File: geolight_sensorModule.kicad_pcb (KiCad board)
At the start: 2 copper layers, 33 x 24.9 mm, 21 parts, among them P2 ICSP, U1 TCRT5000/L

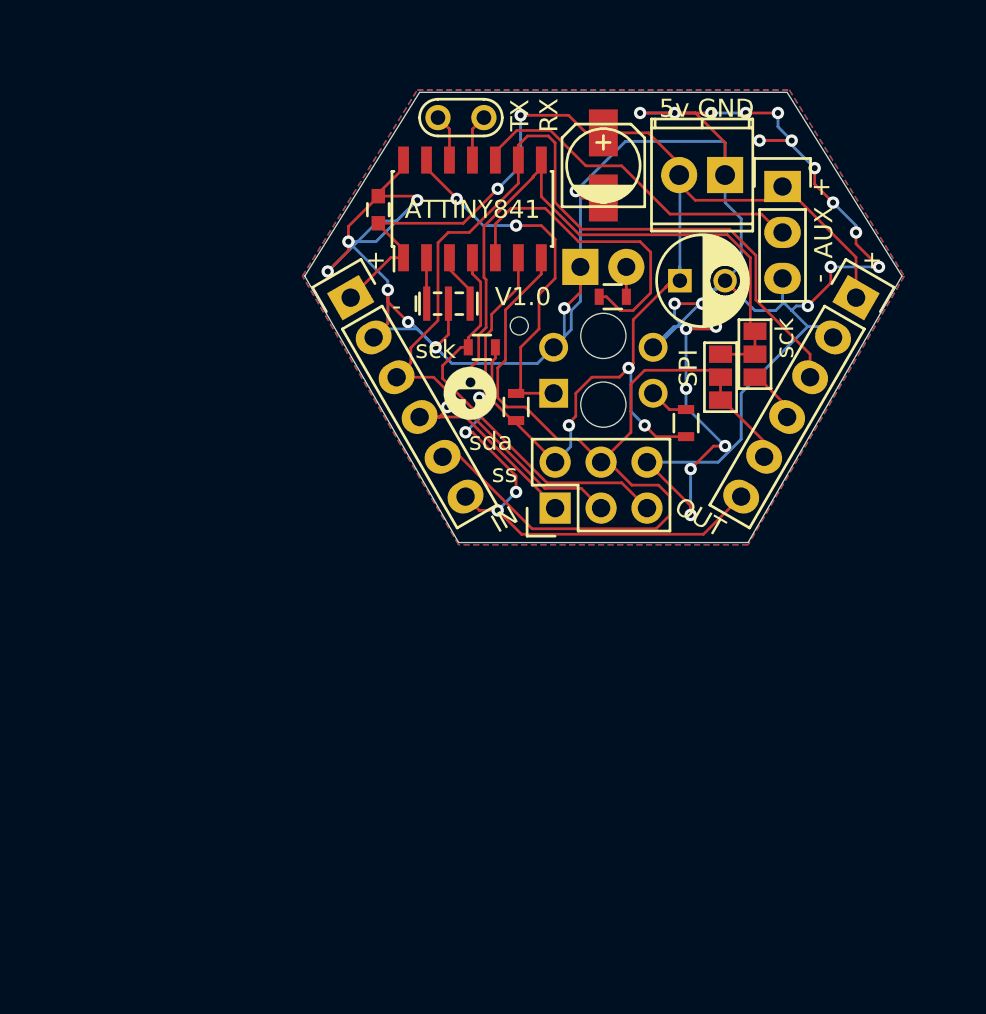
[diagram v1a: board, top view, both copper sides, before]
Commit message: removed empty path cap, changed all 0603 to 0603_handsolder, fixed I2C wiring order, left SPI channels but most likely unused.
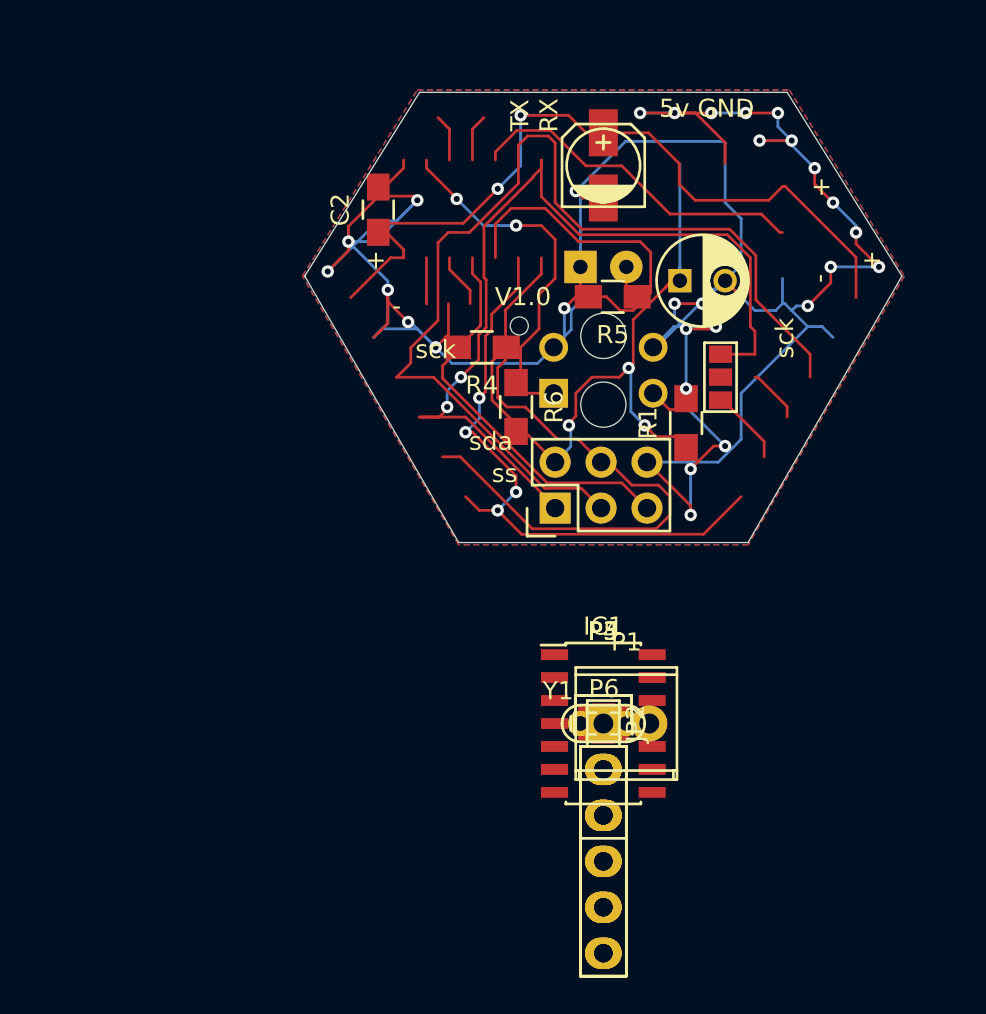
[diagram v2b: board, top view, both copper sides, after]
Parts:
- removed 16M: 16Mhz, Crystals:Resonator_3.2x1.3mm
- removed 5V: 5V, Terminal_Blocks:TerminalBlock_Pheonix_MPT-2.54mm_2pol
- removed ATTINY841: ATTINY841-SSU, Housings_SOIC:SOIC-14_3.9x8.7mm_Pitch1.27mm
- removed AUX: AUX_SENSOR, Pin_Headers:Pin_Header_Straight_1x03
- removed G***: LOGO, Symbols:TI_Logo_F.SilkS_3mm
- removed G***: LOGO, Symbols:TI_Logo_F.SilkS_15mm
- removed IN: IN, Pin_Headers:Pin_Header_Straight_1x06
- removed OUT: OUT, Pin_Headers:Pin_Header_Straight_1x06
- removed SPI: MISO EN, Connect:GS3
- removed tx/rx: UART, Measurement_Points:Test_Point
- added IC1: ATTINY841-SSU, Housings_SOIC:SOIC-14_3.9x8.7mm_Pitch1.27mm, F.Cu at (157.5, 143.4)
- added JP2: OPEN, Connect:GS2, F.Cu at (157.5, 143.4)
- added P1: OPEN, Terminal_Blocks:TerminalBlock_Pheonix_MPT-2.54mm_2pol, F.Cu at (157.5, 143.4)
- added P3, P4: Male Pin Header, Angled (90*), Pin_Headers:Pin_Header_Straight_1x06, F.Cu at (157.5, 143.4)
- added P5: OPEN, Pin_Headers:Pin_Header_Straight_1x03, F.Cu at (157.5, 143.4)
- added P6: OPEN, Measurement_Points:Test_Point, F.Cu at (157.5, 143.4)
- added Y1: 16Mhz, Crystals:Resonator_3.2x1.3mm, F.Cu at (157.5, 143.4)
- C1: value 10-220uF -> OPEN
- C2: footprint Capacitors_SMD:C_0603 -> Capacitors_SMD:C_0805_HandSoldering
- D1: footprint LEDs:LED-3MM -> LEDs:LED-8MM
- JP1: value I2C/SS -> OPEN
- P2: value ICSP -> OPEN
- R1, R5: value 220? -> 220; footprint Resistors_SMD:R_0603 -> Resistors_SMD:R_0805_HandSoldering
- R4, R6: footprint Resistors_SMD:R_0603 -> Resistors_SMD:R_0805_HandSoldering
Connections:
- JP1 pad 2: /SDA/MOSI -> Net-(JP1-Pad2)
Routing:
- net (no net): track 0.00 -> 66.9 mm, vias 0 -> 4
- net /SS: track 33.9 -> 0.00 mm, vias 4 -> 0
- net /AUX: track 19.2 -> 0.00 mm
- net Net-(D1-Pad2): track 1.65 -> 18.9 mm
- net Net-(IC1-Pad5): track 17.6 -> 1.66 mm
- net /SDA/MOSI: track 52.1 -> 40.2 mm
- net Net-(JP2-Pad1): track 3.03 -> 0.00 mm
- net Net-(IC1-Pad3): track 3.01 -> 0.00 mm
- net /TX: track 2.61 -> 0.00 mm
- net /RX: track 2.61 -> 0.00 mm
- net Net-(IC1-Pad2): track 2.55 -> 0.00 mm
- net GND: track 176.4 -> 175.2 mm, vias 30 -> 29
- net Net-(R1-Pad2): vias 0 -> 1

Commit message: 90% complete for 8mm LED. Stopping for change back to 5mm.
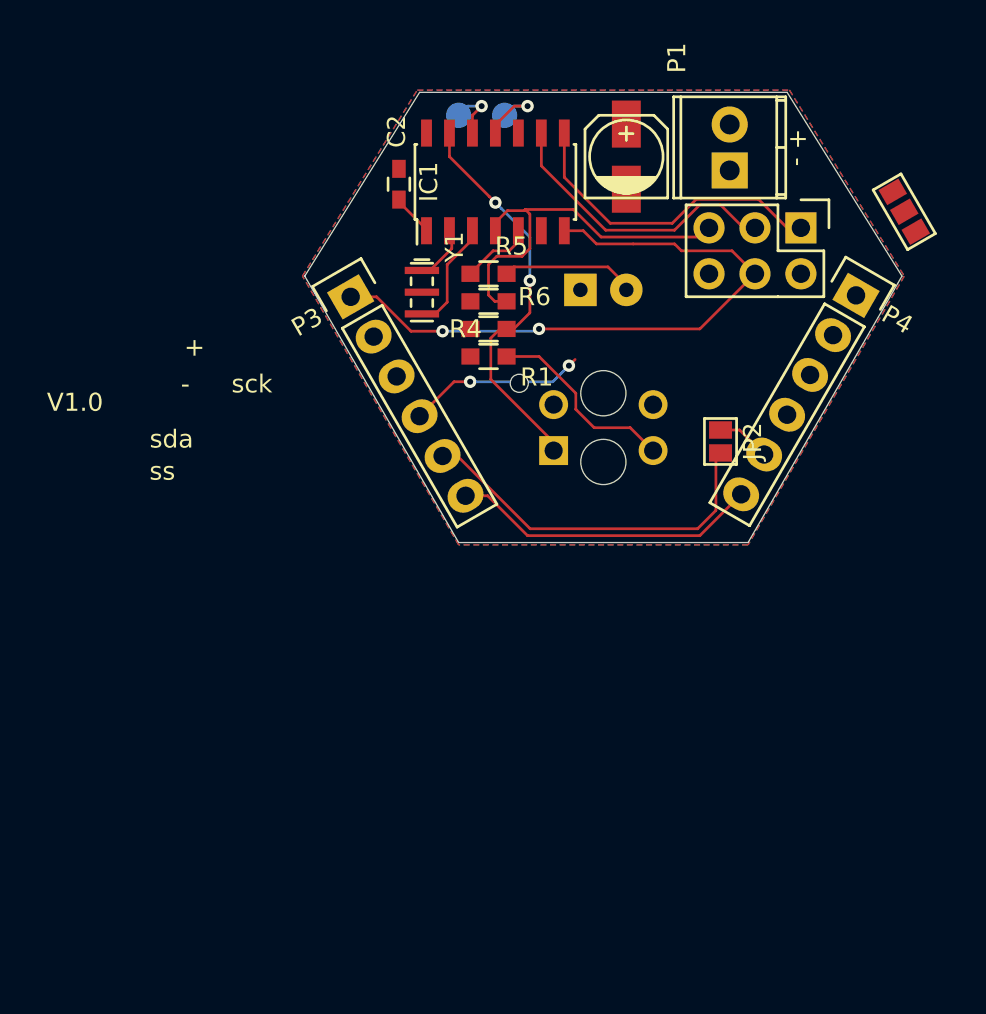
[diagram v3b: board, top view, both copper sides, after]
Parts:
- removed C1: OPEN, Capacitors_ThroughHole:C_Radial_D5_L6_P2.5
- removed P5: OPEN, Pin_Headers:Pin_Header_Straight_1x03
- C2: footprint Capacitors_SMD:C_0805_HandSoldering -> Capacitors_SMD:C_0603_HandSolderingShort
- JP1: value OPEN -> I2C/SPI
- JP2: value OPEN -> MISO_EN
- P1: value OPEN -> 5V inject
- P3: value Male Pin Header, Angled (90*) -> IN
- P4: value Male Pin Header, Angled (90*) -> OUT
- P6: value OPEN -> DEBUG; moved to B.Cu
- R1, R4, R5, R6: footprint Resistors_SMD:R_0805_HandSoldering -> Resistors_SMD:R_0603_HandSolderingShort
- moved P6 34.3 mm to (150.7, 109.7)
- moved P1 31.4 mm to (164.5, 112.8), turned to 90 degrees
- moved IC1 30.5 mm to (151.5, 113.4), turned to 90 degrees
- moved P4 27.5 mm to (171.4, 119.7), turned to 330 degrees
- moved P3 27.4 mm to (143.5, 119.8), turned to 30 degrees
- moved Y1 25.9 mm to (147.4, 119.5), turned to 270 degrees
- moved P2 20.6 mm to (168.4, 116.0), turned to 270 degrees
- moved JP2 16.9 mm to (164.0, 127.8)
- moved JP1 13.7 mm to (174.1, 115.1), turned to 30 degrees
- moved R1 11.5 mm to (151.1, 123.1), turned to 0 degrees
- moved R5 6.99 mm to (151.1, 118.5)
- moved R6 4.58 mm to (151.1, 121.5), turned to 180 degrees
- moved U1 3.17 mm to (157.5, 127.0)
- moved R4 2.57 mm to (151.1, 120.0), turned to 0 degrees
- moved C2 1.81 mm to (146.2, 113.5)
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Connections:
- P4 pad 1: /SCK/SCL -> Net-(JP1-Pad2)
- P4 pad 4: Net-(JP1-Pad2) -> /SCK/SCL
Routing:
- net GND: track 175.2 -> 0.00 mm, vias 29 -> 0
- net +5V: track 79.8 -> 2.35 mm, vias 5 -> 0
- net (no net): track 66.9 -> 0.00 mm, vias 4 -> 0
- net /SCK/SCL: track 56.6 -> 26.1 mm, vias 0 -> 2
- net /SS: track 0.00 -> 17.6 mm
- net Net-(D1-Pad2): track 18.9 -> 7.45 mm
- net /MISO: track 49.7 -> 38.3 mm, vias 2 -> 0
- net Net-(R1-Pad2): track 2.20 -> 10.8 mm, vias 1 -> 0
- net Net-(IC1-Pad3): track 0.00 -> 6.19 mm
- net /SDA/MOSI: track 40.2 -> 36.0 mm, vias 0 -> 2
- net /RX: track 0.00 -> 4.14 mm, vias 0 -> 1
- net Net-(IC1-Pad2): track 0.00 -> 3.19 mm
- net /TX: track 0.00 -> 3.18 mm, vias 0 -> 1
- net Net-(JP2-Pad1): track 0.00 -> 2.97 mm
- net Net-(IC1-Pad5): track 1.66 -> 4.00 mm
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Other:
- board text added: "+ -"
- board text added: "RX|TX"
- board text removed: "5v GND"
- board text removed: "TX RX"

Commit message: 5mm, rev2 stage (wait a day and finalize)
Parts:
- added P5: AUX Sensor, Pin_Headers:Pin_Header_Straight_1x03, F.Cu at (160.0, 131.1)
- D1: footprint LEDs:LED-8MM -> LEDs:LED-5MM
- JP1: footprint Connect:GS3 -> Connect:GS2
- JP2: footprint Connect:GS2 -> Measurement_Points:Measurement_Point_Square-SMD-Pad_SmallRect
- moved JP2 11.2 mm to (169.5, 118.1), turned to 180 degrees
- moved JP1 4.71 mm to (169.5, 116.2), turned to 0 degrees
- moved U1 1.65 mm to (157.5, 125.3)
- moved P2 1.42 mm to (167.0, 116.2)
- moved R6 0.92 mm to (150.2, 121.8)
- moved R1 0.92 mm to (150.2, 123.3)
- moved P6 0.51 mm to (150.7, 110.2)
- moved Y1 0.25 mm to (147.4, 119.3)
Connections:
- JP1 pad 1: /MISO -> /SDA/MOSI
- JP1 pad 2: Net-(JP1-Pad2) -> /SDA/MOSI
- P4 pad 1: Net-(JP1-Pad2) -> /SDA/MOSI
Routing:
- net GND: track 0.00 -> 129.2 mm, vias 0 -> 45
- net +5V: track 2.35 -> 69.2 mm, vias 0 -> 5
- net /AUX: track 0.00 -> 32.7 mm, vias 0 -> 4
- net /SS: track 17.6 -> 49.5 mm, vias 0 -> 2
- net /SCK/SCL: track 26.1 -> 52.9 mm, vias 2 -> 1
- net Net-(JP2-Pad1): track 2.97 -> 13.4 mm
- net /SDA/MOSI: track 36.0 -> 46.3 mm
- net /MISO: track 38.3 -> 45.9 mm, vias 0 -> 1
- net Net-(R1-Pad2): track 10.8 -> 14.1 mm
- net /RESET: track 21.4 -> 19.5 mm
- net Net-(IC1-Pad13): track 22.2 -> 21.2 mm

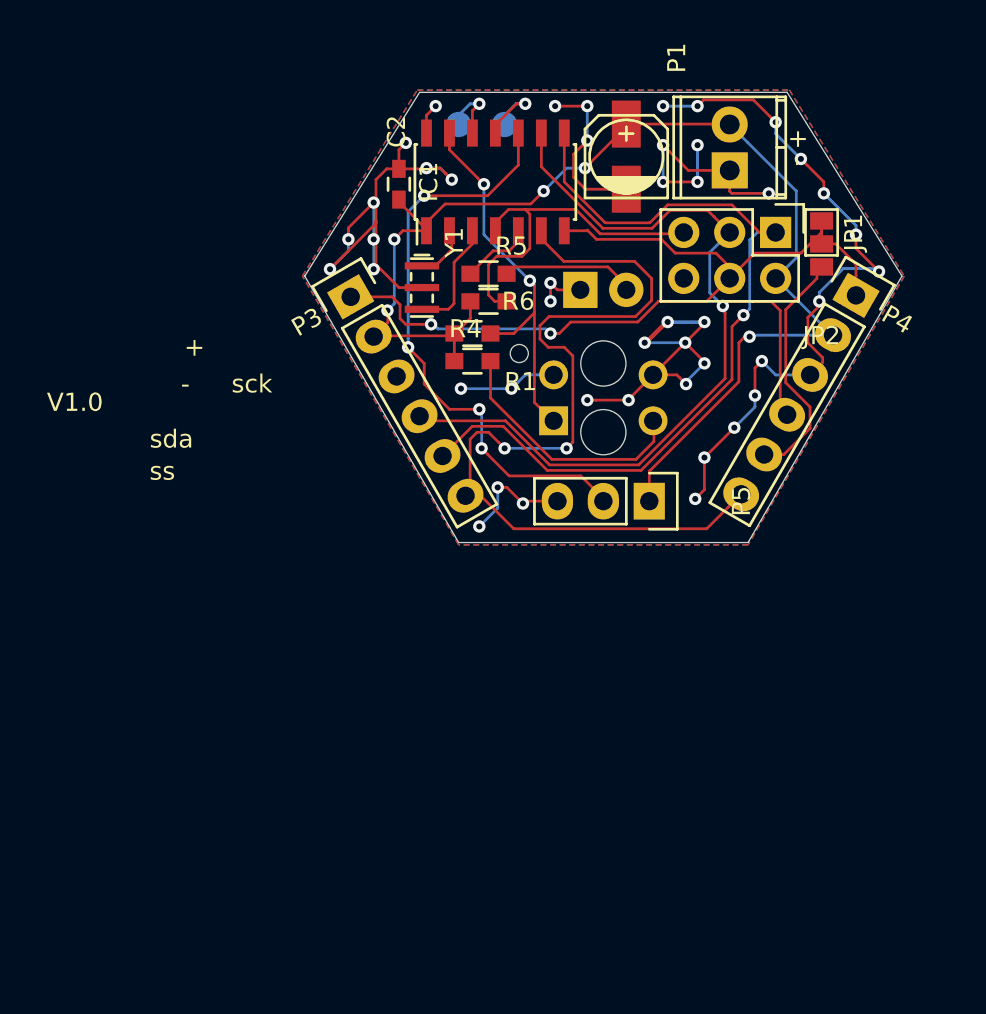
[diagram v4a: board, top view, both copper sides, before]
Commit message: improved ground planes, revised labels/silk
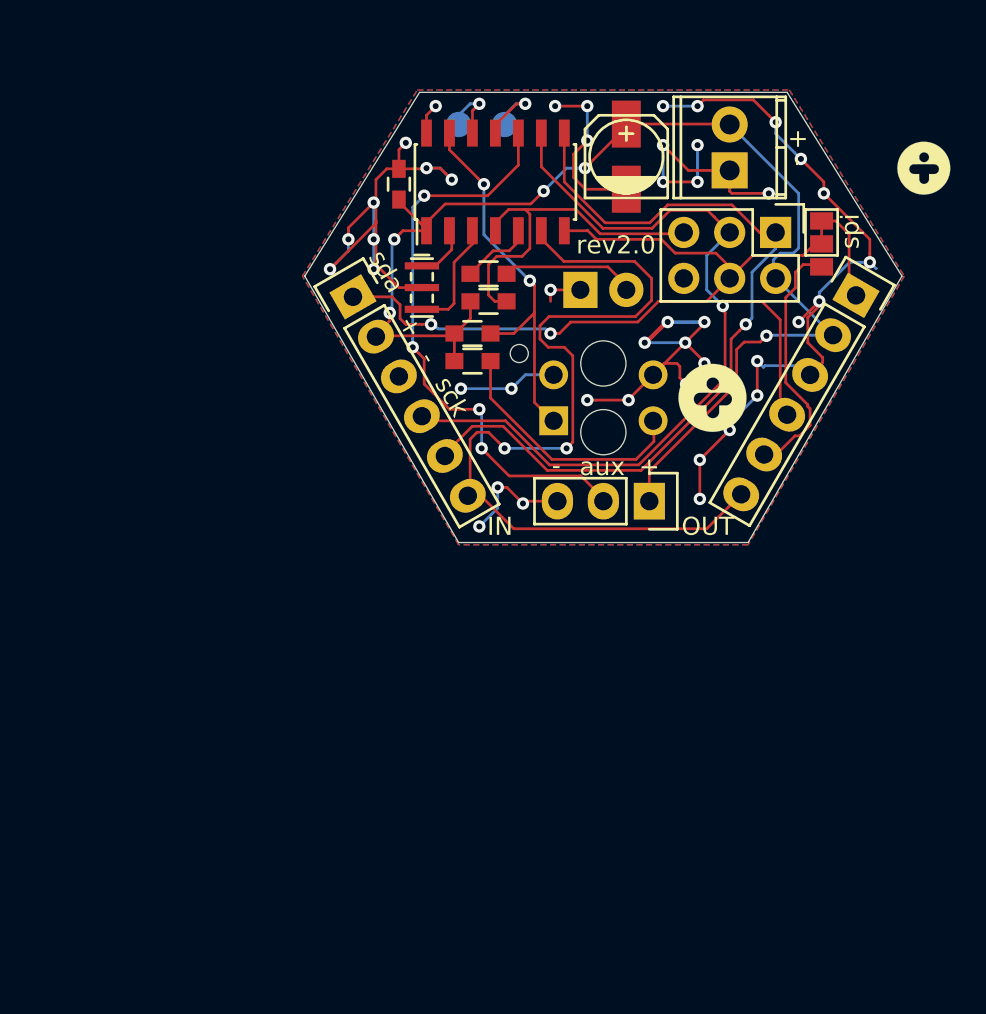
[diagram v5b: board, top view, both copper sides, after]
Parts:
- added G***: LOGO, Symbols:TI_Logo_F.SilkS_15mm, B.Cu at (153.5, 113.4)
- added G***: LOGO, Symbols:TI_Logo_F.SilkS_3mm, F.Cu at (175.2, 112.6)
- added G***: LOGO, Symbols:TI_Logo_F.SilkS_4mm, F.Cu at (163.5, 125.3)
- moved IN 0.13 mm to (143.6, 119.8)
- renumbered P3 to IN, P4 to OUT, JP1 to spi, D1 to white
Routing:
- net GND: track 129.2 -> 130.6 mm, vias 45 -> 44
- net Net-(JP2-Pad1): track 13.4 -> 14.1 mm
- net +5V: track 69.2 -> 69.8 mm
- net /MISO: track 45.9 -> 45.3 mm
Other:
- board text added: "IN"
- board text added: "OUT"
- board text added: "aux"
- board text added: "geodome rev 2.0"
- board text added: "rev2.0"
- board text added: "rx|tx"
- board text removed: "RX|TX"
- board text removed: "V1.0"
- board text removed: "geodome rev 1.0"
- board text removed: "ss"

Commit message: rev2 final staging probably (minor tweaks, fixed SPI option jumpers)
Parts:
- removed the G*** at (175.2, 112.6)
- added JP2: MISO_EN, Measurement_Points:Measurement_Point_Square-SMD-Pad_SmallRect, F.Cu at (169.5, 115.6)
- moved JP2 3.75 mm to (169.5, 114.4)
- moved G*** 2.27 mm to (164.0, 123.1)
- moved spi 1.21 mm to (169.5, 117.4)
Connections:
- JP2 pad 1: Net-(JP2-Pad1) -> /MISO
- OUT pad 5: Net-(JP2-Pad1) -> /MISO
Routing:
- net /MISO: track 45.3 -> 69.5 mm, vias 1 -> 3
- net Net-(JP2-Pad1): track 14.1 -> 0.00 mm
- net GND: track 130.6 -> 117.2 mm, vias 44 -> 41
- net /SDA/MOSI: track 46.6 -> 43.9 mm
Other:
- board text added: "2.0"
- board text removed: "rev2.0"
